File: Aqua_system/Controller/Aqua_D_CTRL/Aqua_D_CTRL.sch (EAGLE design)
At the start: 234 parts, among them IC1 SN65HVD3082EDR, IC2 CSTNE8M00G520000R0, IC3 LT6106CS5#TRPBF, IC4 LT6106CS5#TRPBF, IC5 TPS54202DDCR, IC6 LD1117S33TR, IC8 LM317AEMP, J1 ESP32-PICO-KIT, K1 KB20C06A, K2 KB20C06A, Q1 DMP6185SEQ-13, Q10 BC817, Q11 2N7002, Q12 DMP6185SEQ-13, Q13 2N7002, Q14 DMP6185SEQ-13, Q15 2N7002, Q16 DMP6185SEQ-13, Q17 BC817, Q18 BC817, Q19 BC817, Q2 2N7002, Q20 BC817, Q21 BC817, Q22 BC817, Q23 BC817, Q3 DMP6185SEQ-13, Q4 2N7002, Q5 DMP6185SEQ-13, Q6 DMP6185SEQ-13, Q7 2N7002, Q8 DMP6185SEQ-13, Q9 2N7002, SW1 L101011MS02Q, U2 R7FA6M5BG3CFBLQFP-144-M, X1 B2B-XH-AM(LF)(SN), X10 726386-2TE_726386-2, X11 282834-2, X12 615008148521, X13 MICROMATCH-16, X14 615008148521, X2 WF2549-2WS05S0B01, X3 282834-3, X4 282834-3, X5 726386-2TE_726386-2, X6 726386-2TE_726386-2, X7 726386-2TE_726386-2, X8 726386-2TE_726386-2, X9 726386-2TE_726386-2

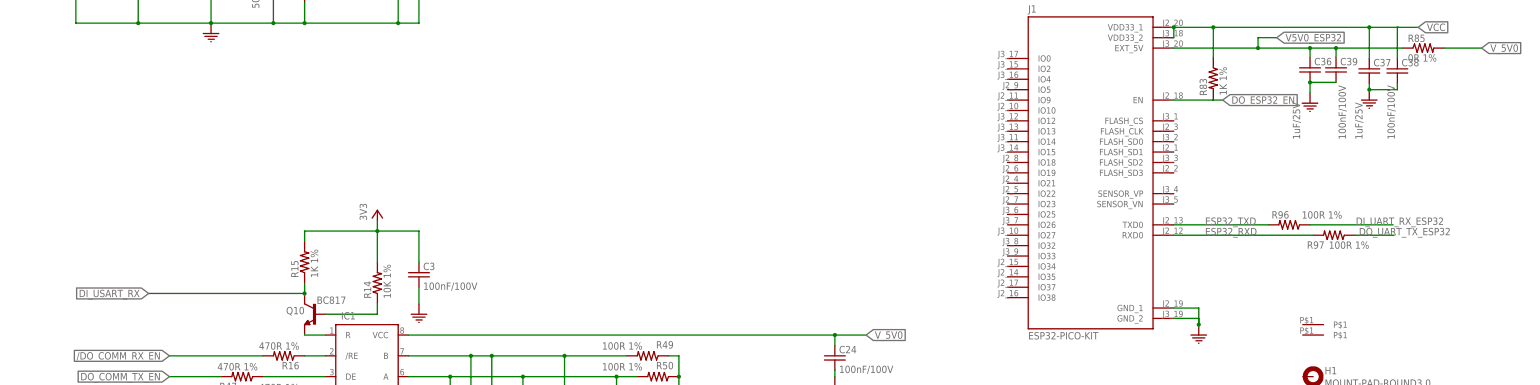
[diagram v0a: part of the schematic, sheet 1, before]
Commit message: HW02.02
Improvements after HW Functional Testing
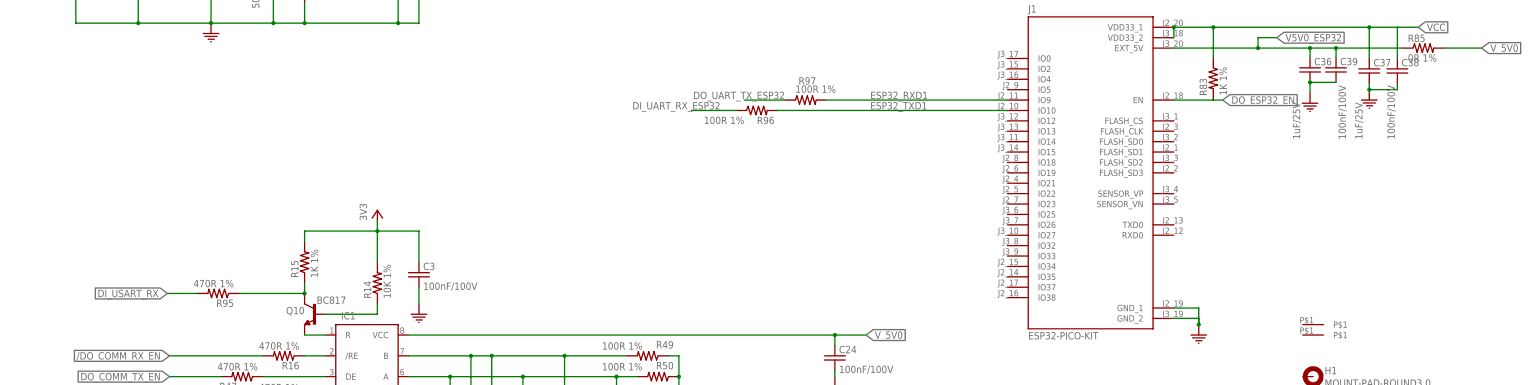
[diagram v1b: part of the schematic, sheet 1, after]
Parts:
- removed K2: KB20C06A, Labops_Lib_AH:KB20C06A
- added C42, C43: 10pF/100V, Labops_Lib_AH:C_0603
- added D14, D15, D16, D17: MMBZ4696-HE3-18, Labops_Lib_AH:MMBZ4696-HE3-18
- added K3: RP1A48D6, Labops_Lib_AH:RP1A48D6
- added R95: 470R 1%, Labops_Lib_AH:R_0603
- K1: value KB20C06A -> RP1A48D6; device Labops_Lib_AH:KB20C06A -> Labops_Lib_AH:RP1A48D6
- Q1, Q12, Q14, Q16, Q3, Q6, Q8: value DMP6185SEQ-13 -> UT2955G-AA3-R; device Labops_Lib_AH:DMP6185SEQ-13 -> Labops_Lib_AH:UT2955G-AA3-R
- R58, R62, R66: value 10K 1% -> 100R 1%
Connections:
- removed net ESP32_RXD: J1.RXD0, R97.2
- removed net ESP32_TXD: J1.TXD0, R96.2
- new net ESP32_RXD1: J1.IO9, R97.2
- new net ESP32_TXD1: J1.IO10, R96.2
- new net N$59: Q10.C, R15.1, R95.1
- net CONDUCTIV_PUMP_MAINS_L_SW: now also K3.3; no longer K2.3
- net DI_USART_RX: now also R95.2; no longer Q10.C, R15.1
- net DO_7XSEGMENT_1_EN: now also R60.1, U2A.P402; no longer R56.1, U2A.P400
- net DO_7XSEGMENT_3_EN: now also R56.1, U2A.P400; no longer R60.1, U2A.P402
- net GND: now also C42.1, C43.1, K3.1; no longer K2.1
- net MAINS_L_F: now also K3.4; no longer K2.4
- net N$11: now also D15.A
- net N$13: now also D16.A
- net N$21: now also D17.A
- net N$3: now also D14.A
- net N$49: now also C43.2
- net N$5: now also K3.2; no longer K2.2
- net N$66: now also C42.2
- net V_24V0_P: now also D14.C, D15.C, D16.C, D17.C
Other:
- moved on the sheet: C50, R96, R97
